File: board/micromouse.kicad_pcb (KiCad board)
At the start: 2 copper layers, 50 x 72 mm, 66 parts, among them J1 PowerBtnLower, J12 MotorsUpper, J2 SERIAL, J3 PWR_SEL, J4 Front Sense, J5 Left Sense, J6 Right Sense, J7 Back Sense, J8 PowerBtnUpper, J9 MotorsLower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

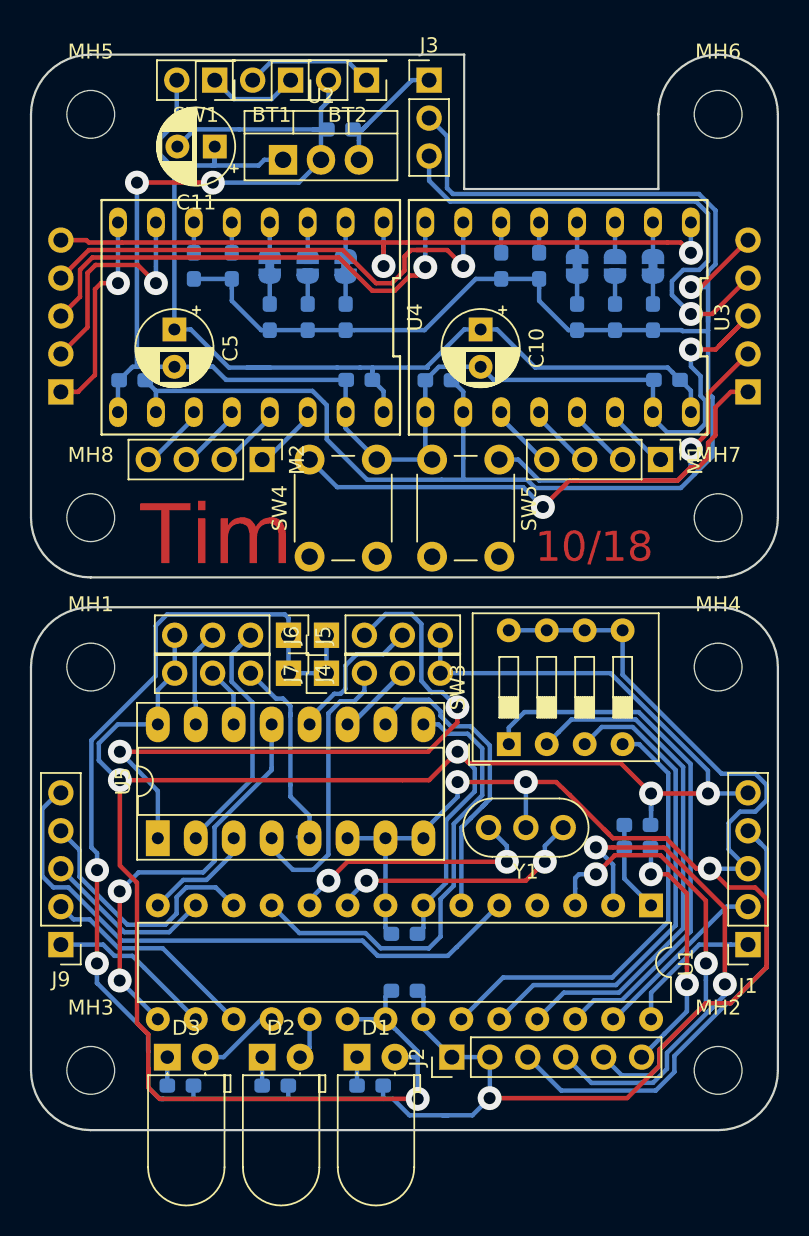
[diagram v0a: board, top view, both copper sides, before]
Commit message: Final 2-board design
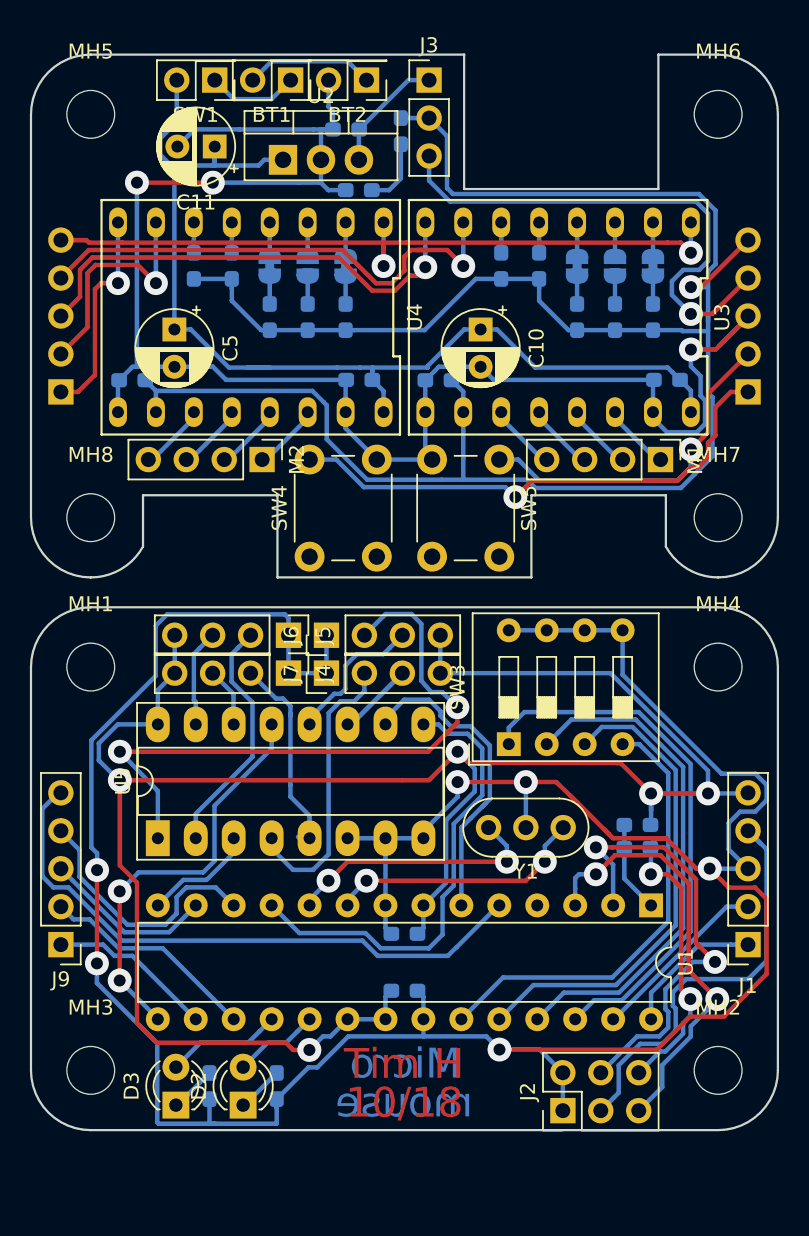
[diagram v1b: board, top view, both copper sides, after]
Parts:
- D1: footprint LED_THT:LED_D5.0mm_Horizontal_O1.27mm_Z3.0mm -> LED_SMD:LED_0603_1608Metric_Pad1.05x0.95mm_HandSolder; moved to B.Cu
- D2, D3: footprint LED_THT:LED_D5.0mm_Horizontal_O1.27mm_Z3.0mm -> LED_THT:LED_D3.0mm
- J2: footprint Connector_PinHeader_2.54mm:PinHeader_1x06_P2.54mm_Vertical -> Connector_PinHeader_2.54mm:PinHeader_2x03_P2.54mm_Vertical
- moved D1 62.1 mm to (149.8, 69.1), turned to 90 degrees
- moved R12 59.9 mm to (146.9, 73.1), turned to 180 degrees
- moved J2 8.25 mm to (160.6, 134.7)
- moved D2 3.45 mm to (139.2, 134.3), turned to 90 degrees
- moved D3 3.26 mm to (134.7, 134.3), turned to 90 degrees
- moved R14 1.95 mm to (136.9, 133.1), turned to 270 degrees
- moved C8 0.41 mm to (146.1, 69.0)
- moved R13 0.10 mm to (141.4, 133.1), turned to 270 degrees
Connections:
- D1 pad 2: +5VD -> +5V
- R12 pad 2: GNDD -> GND
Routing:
- net +5VD: track 153.5 -> 137.2 mm
- net /RX: track 35.3 -> 30.5 mm
- net GND: track 110.7 -> 113.8 mm
- net /LED1: track 2.80 -> 5.78 mm
- net /USB_5V: track 31.8 -> 28.9 mm
- net GNDD: track 196.4 -> 199.2 mm
- net Net-(D1-Pad1): track 1.91 -> 4.56 mm
- net /LED2: track 5.50 -> 7.74 mm
- net Net-(C9-Pad2): track 16.9 -> 18.9 mm
- net +5V: track 140.1 -> 142.0 mm
- net Net-(D3-Pad1): track 1.91 -> 3.14 mm
- net Net-(D2-Pad1): track 1.91 -> 3.14 mm
- net Net-(C8-Pad1): track 8.96 -> 8.09 mm
- net /BTN1_T: track 35.8 -> 35.0 mm
- net /SENSE_TRIG: track 26.9 -> 27.5 mm
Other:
- outline, holes or cut-outs redrawn
- board text added: "Micro"
- board text added: "Tim H"
- board text added: "mouse"
- board text removed: "Tim"
